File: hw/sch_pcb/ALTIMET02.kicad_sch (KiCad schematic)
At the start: 14 parts, among them IC1 MS561101BA03-50, J2 HEADER_2x03, J3 HEADER_2x05_PARALLEL

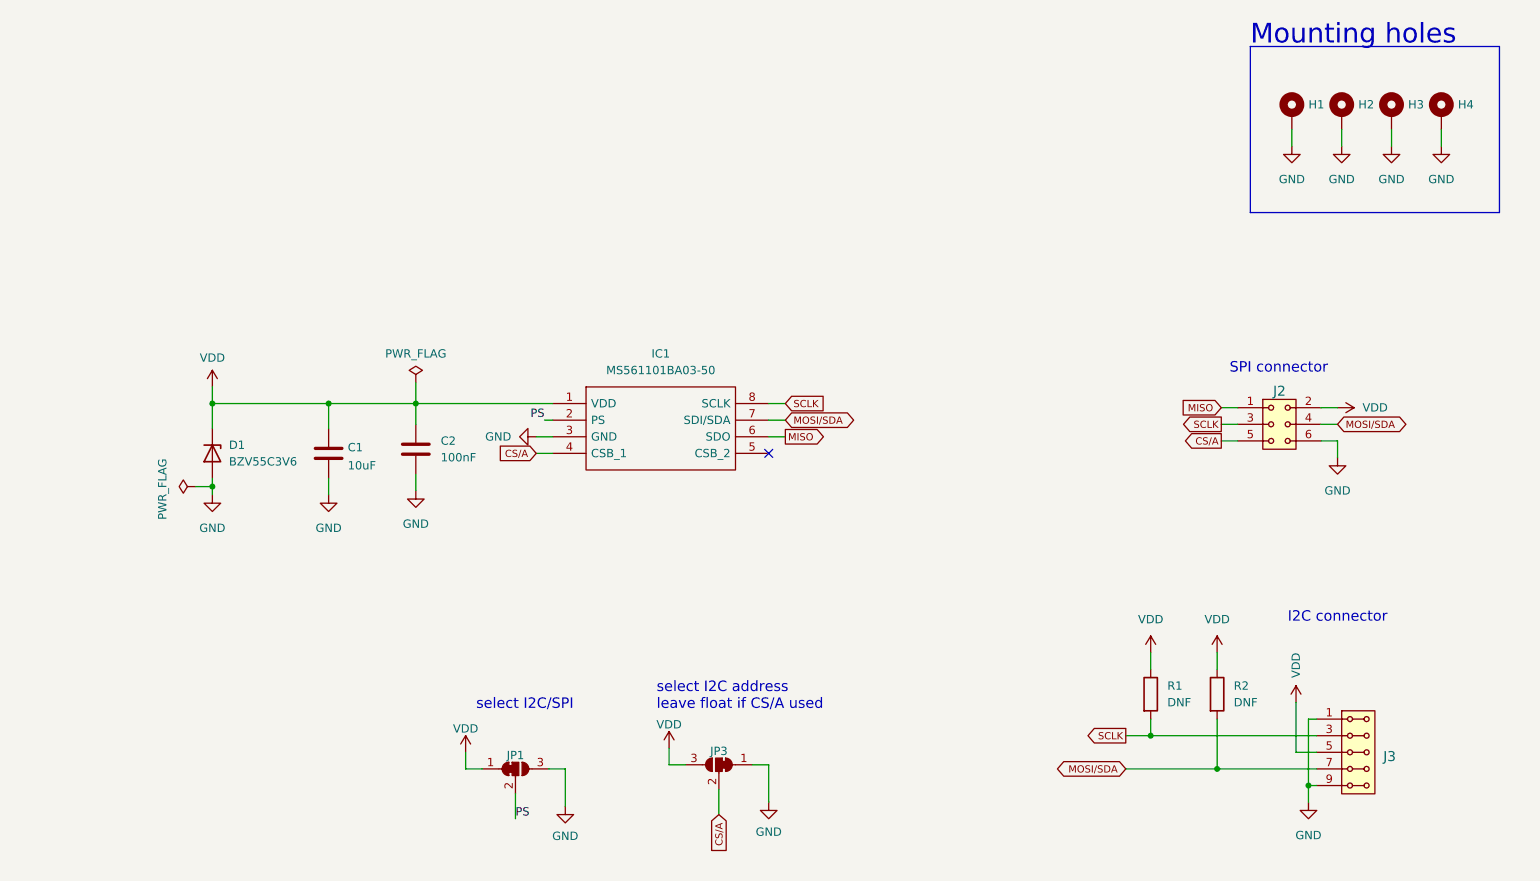
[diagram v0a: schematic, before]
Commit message: power connector added, SPI and I2C connectors modified, default I2C adrress changed
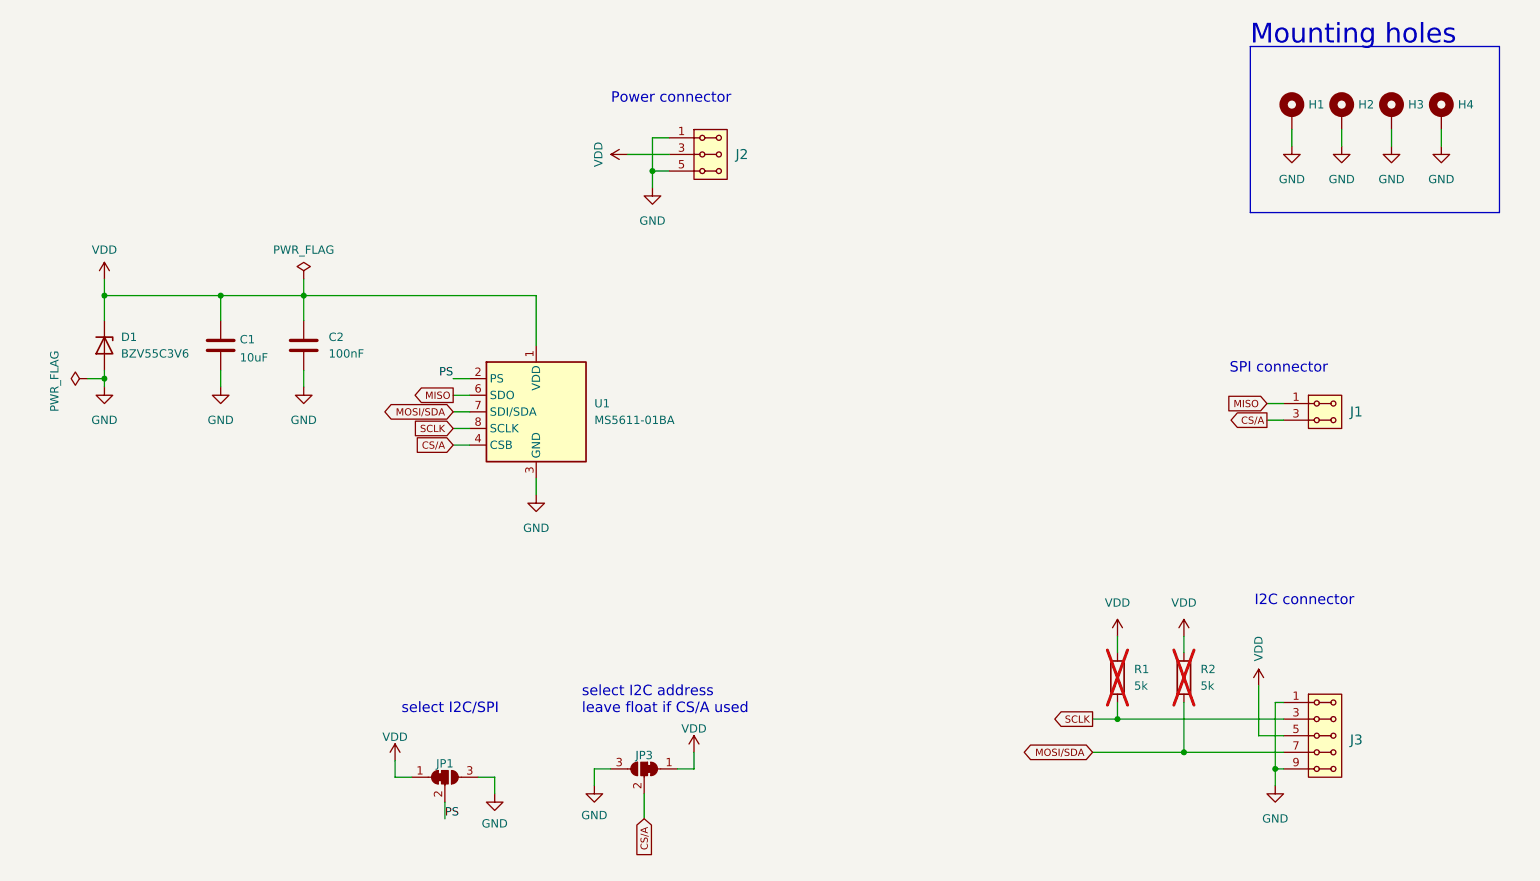
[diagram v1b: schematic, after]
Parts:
- removed IC1: MS561101BA03-50, KiCad:MS561101BA03-50, symbol MS561101BA03-50:MS561101BA03-50
- removed J2: HEADER_2x03, Mlab_Pin_Headers:Straight_2x03, symbol MLAB_HEADER:HEADER_2x03
- added J1: HEADER_2x02_PARALLEL, Mlab_Pin_Headers:Straight_2x02, symbol MLAB_HEADER:HEADER_2x02_PARALLEL
- added J2: HEADER_2x03_PARALLEL, Mlab_Pin_Headers:Straight_2x03, symbol MLAB_HEADER:HEADER_2x03_PARALLEL
- added U1: MS5611-01BA, Package_LGA:LGA-8_3x5mm_P1.25mm, symbol Sensor_Pressure:MS5611-01BA
- R1, R2: value DNF -> 5k; now not fitted
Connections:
- net CS/A: now also J1.3, J1.4, U1.4 (CSB), U1.5 (CSB)
- net GND: now also JP3.3 (B), J2.1, J2.2, J2.5, J2.6, U1.3 (GND); no longer JP3.1 (A)
- net MISO: now also J1.1, J1.2, U1.6 (SDO)
- net MOSI/SDA: now also U1.7 (SDI/SDA)
- net PS: now also U1.2 (PS)
- net SCLK: now also U1.8 (SCLK)
- net VDD: now also JP3.1 (A), J2.3, J2.4, U1.1 (VDD); no longer JP3.3 (B)
- no-connect marks 1 -> 0
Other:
- note added: "Power connector"
- moved on the sheet: C1, C2, D1, J3, JP1, JP3

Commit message: minor changes in layout, change diode
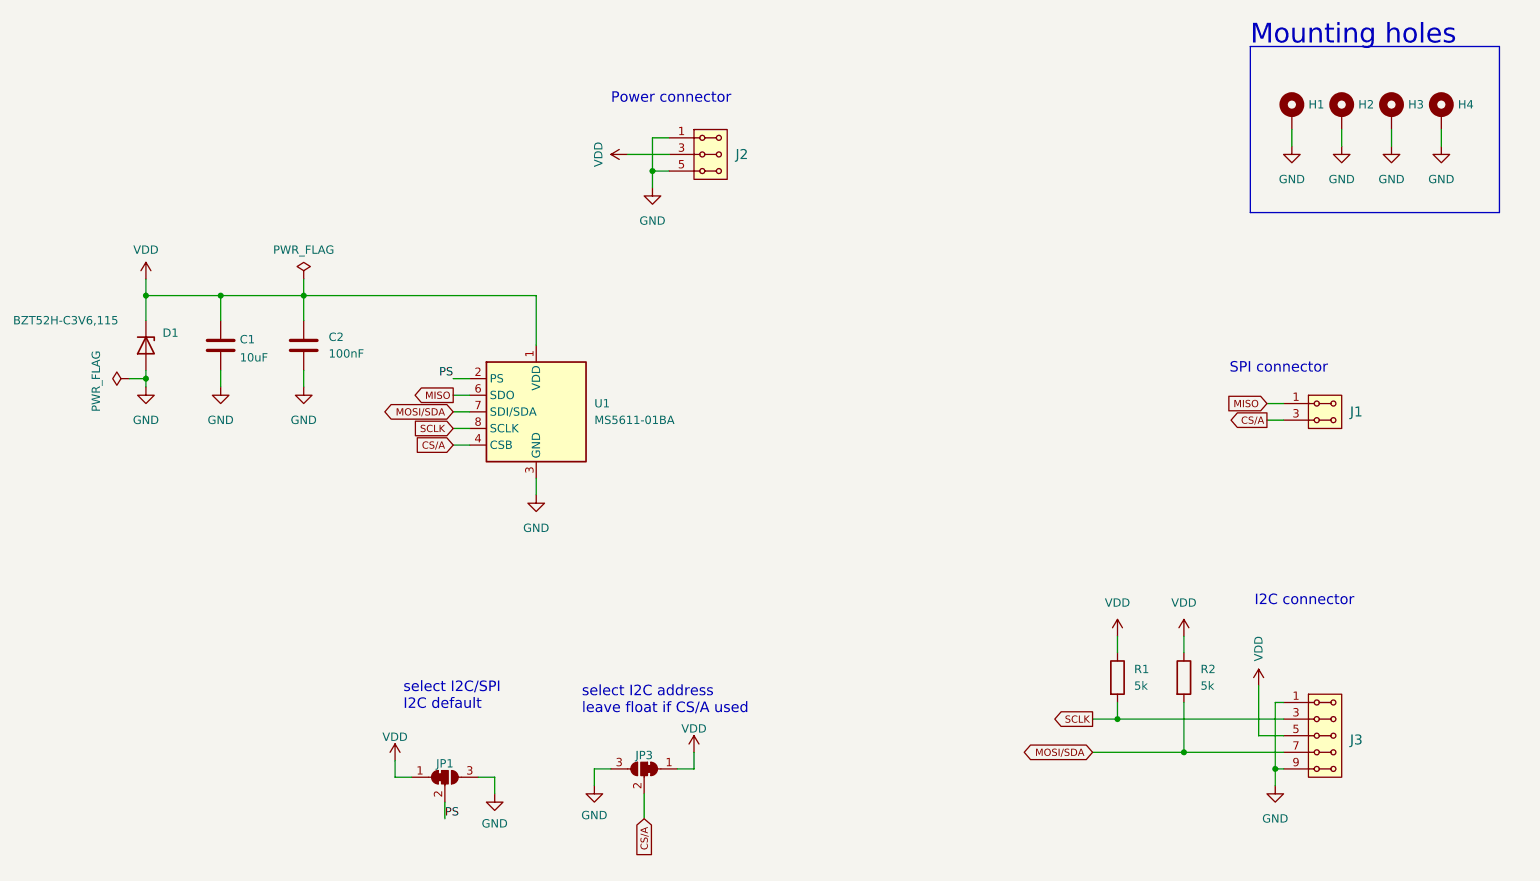
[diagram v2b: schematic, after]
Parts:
- D1: value BZV55C3V6 -> BZT52H-C3V6,115; footprint Mlab_D:Diode-MiniMELF_Standard -> Diode_SMD:D_SOD-123F
- R1, R2: now fitted
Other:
- note added: "select I2C/SPI I2C default"
- note removed: "select I2C/SPI"
- moved on the sheet: D1
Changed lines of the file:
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@@
   (junction (at 95.25 59.69) (diameter 0) (color 0 0 0 0)
   )
-  (junction (at 64.77 72.39) (diameter 0) (color 0 0 0 0)
+  (junction (at 71.12 72.39) (diameter 0) (color 0 0 0 0)
   )
   (junction (at 243.84 132.08) (diameter 0) (color 0 0 0 0)
@@
   (junction (at 219.71 124.46) (diameter 0) (color 0 0 0 0)
   )
-  (junction (at 64.77 59.69) (diameter 0) (color 0 0 0 0)
+  (junction (at 71.12 59.69) (diameter 0) (color 0 0 0 0)
   )
   (wire (pts (xy 82.55 59.69) (xy 82.55 63.5))
@@
     (stroke (width 0) (type default))
   )
-  (wire (pts (xy 62.23 72.39) (xy 64.77 72.39))
+  (wire (pts (xy 68.58 72.39) (xy 71.12 72.39))
     (stroke (width 0) (type default))
   )
@@
     (stroke (width 0) (type default))
   )
-  (wire (pts (xy 64.77 57.15) (xy 64.77 59.69))
+  (wire (pts (xy 71.12 57.15) (xy 71.12 59.69))
     (stroke (width 0) (type default))
   )
@@
     (stroke (width 0) (type default))
   )
-  (wire (pts (xy 64.77 72.39) (xy 64.77 73.66))
+  (wire (pts (xy 71.12 72.39) (xy 71.12 73.66))
     (stroke (width 0) (type default))
   )
@@
     (stroke (width 0) (type default))
   )
-  (wire (pts (xy 64.77 59.69) (xy 82.55 59.69))
+  (wire (pts (xy 71.12 59.69) (xy 82.55 59.69))
     (stroke (width 0) (type default))
   )
@@
     (stroke (width 0) (type default))
   )
-  (wire (pts (xy 64.77 63.5) (xy 64.77 59.69))
+  (wire (pts (xy 71.12 63.5) (xy 71.12 59.69))
     (stroke (width 0) (type default))
   )
@@
     (stroke (width 0) (type default))
   )
-  (wire (pts (xy 64.77 71.12) (xy 64.77 72.39))
+  (wire (pts (xy 71.12 71.12) (xy 71.12 72.39))
     (stroke (width 0) (type default))
   )
@@
     (stroke (width 0) (type default))
   )
-  (text "select I2C/SPI" (at 125.095 123.825 0)
-    (effects (font (size 1.6 1.6)) (justify right bottom))
+  (text "select I2C/SPI\nI2C default" (at 110.49 123.19 0)
+    (effects (font (size 1.6 1.6)) (justify left bottom))
   )
   (text "Mounting holes" (at 240.03 21.59 0)
@@
     )
   )
-  (symbol (lib_id "Device:D_Zener") (at 64.77 67.31 270) (unit 1)
-    (in_bom yes) (on_board yes) (dnp no) (fields_autoplaced)
-    (property "Reference" "D1" (at 67.31 66.0399 90)
-      (effects (font (size 1.27 1.27)) (justify left))
-    )
-    (property "Value" "BZV55C3V6" (at 67.31 68.5799 90)
-      (effects (font (size 1.27 1.27)) (justify left))
-    )
-    (property "Footprint" "Mlab_D:Diode-MiniMELF_Standard" (at 64.77 67.31 0)
-      (effects (font (size 1.27 1.27)) hide)
-    )
-    (property "Datasheet" "~" (at 64.77 67.31 0)
+  (symbol (lib_id "Device:D_Zener") (at 71.12 67.31 270) (unit 1)
+    (in_bom yes) (on_board yes) (dnp no)
+    (property "Reference" "D1" (at 73.66 65.405 90)
+      (effects (font (size 1.27 1.27)) (justify left))
+    )
+    (property "Value" "BZT52H-C3V6,115" (at 50.8 63.5 90)
+      (effects (font (size 1.27 1.27)) (justify left))
+    )
+    (property "Footprint" "Diode_SMD:D_SOD-123F" (at 71.12 67.31 0)
+      (effects (font (size 1.27 1.27)) hide)
+    )
+    (property "Datasheet" "~" (at 71.12 67.31 0)
       (effects (font (size 1.27 1.27)) hide)
     )
@@
     )
   )
-  (symbol (lib_id "power:GND") (at 64.77 73.66 0) (unit 1)
-    (in_bom yes) (on_board yes) (dnp no) (fields_autoplaced)
-    (property "Reference" "#PWR01" (at 64.77 80.01 0)
-      (effects (font (size 1.27 1.27)) hide)
-    )
-    (property "Value" "GND" (at 64.77 78.74 0)
-      (effects (font (size 1.27 1.27)))
-    )
-    (property "Footprint" "" (at 64.77 73.66 0)
-      (effects (font (size 1.27 1.27)) hide)
-    )
-    (property "Datasheet" "" (at 64.77 73.66 0)
+  (symbol (lib_id "power:GND") (at 71.12 73.66 0) (unit 1)
+    (in_bom yes) (on_board yes) (dnp no) (fields_autoplaced)
+    (property "Reference" "#PWR01" (at 71.12 80.01 0)
+      (effects (font (size 1.27 1.27)) hide)
+    )
+    (property "Value" "GND" (at 71.12 78.74 0)
+      (effects (font (size 1.27 1.27)))
+    )
+    (property "Footprint" "" (at 71.12 73.66 0)
+      (effects (font (size 1.27 1.27)) hide)
+    )
+    (property "Datasheet" "" (at 71.12 73.66 0)
       (effects (font (size 1.27 1.27)) hide)
     )
@@
   )
   (symbol (lib_id "Device:R") (at 229.87 118.11 0) (unit 1)
-    (in_bom yes) (on_board yes) (dnp yes) (fields_autoplaced)
+    (in_bom yes) (on_board yes) (dnp no) (fields_autoplaced)
     (property "Reference" "R2" (at 232.41 116.84 0)
       (effects (font (size 1.27 1.27)) (justify left))
@@
     )
   )
-  (symbol (lib_id "power:PWR_FLAG") (at 62.23 72.39 90) (unit 1)
+  (symbol (lib_id "power:PWR_FLAG") (at 68.58 72.39 90) (unit 1)
     (in_bom yes) (on_board yes) (dnp no)
-    (property "Reference" "#FLG02" (at 60.325 72.39 0)
-      (effects (font (size 1.27 1.27)) hide)
-    )
-    (property "Value" "PWR_FLAG" (at 57.15 77.47 0)
-      (effects (font (size 1.27 1.27)) (justify left))
-    )
-    (property "Footprint" "" (at 62.23 72.39 0)
-      (effects (font (size 1.27 1.27)) hide)
-    )
-    (property "Datasheet" "~" (at 62.23 72.39 0)
+    (property "Reference" "#FLG02" (at 66.675 72.39 0)
+      (effects (font (size 1.27 1.27)) hide)
+    )
+    (property "Value" "PWR_FLAG" (at 63.5 77.47 0)
+      (effects (font (size 1.27 1.27)) (justify left))
+    )
+    (property "Footprint" "" (at 68.58 72.39 0)
+      (effects (font (size 1.27 1.27)) hide)
+    )
+    (property "Datasheet" "~" (at 68.58 72.39 0)
       (effects (font (size 1.27 1.27)) hide)
     )
@@
     )
   )
-  (symbol (lib_id "power:VDD") (at 64.77 57.15 0) (unit 1)
+  (symbol (lib_id "power:VDD") (at 71.12 57.15 0) (unit 1)
     (in_bom yes) (on_board yes) (dnp no)
-    (property "Reference" "#PWR02" (at 64.77 60.96 0)
-      (effects (font (size 1.27 1.27)) hide)
-    )
-    (property "Value" "VDD" (at 64.77 52.705 0)
-      (effects (font (size 1.27 1.27)))
-    )
-    (property "Footprint" "" (at 64.77 57.15 0)
-      (effects (font (size 1.27 1.27)) hide)
-    )
-    (property "Datasheet" "" (at 64.77 57.15 0)
+    (property "Reference" "#PWR02" (at 71.12 60.96 0)
+      (effects (font (size 1.27 1.27)) hide)
+    )
+    (property "Value" "VDD" (at 71.12 52.705 0)
+      (effects (font (size 1.27 1.27)))
+    )
+    (property "Footprint" "" (at 71.12 57.15 0)
+      (effects (font (size 1.27 1.27)) hide)
+    )
+    (property "Datasheet" "" (at 71.12 57.15 0)
       (effects (font (size 1.27 1.27)) hide)
     )
@@
   )
   (symbol (lib_id "Device:R") (at 219.71 118.11 0) (unit 1)
-    (in_bom yes) (on_board yes) (dnp yes) (fields_autoplaced)
+    (in_bom yes) (on_board yes) (dnp no) (fields_autoplaced)
     (property "Reference" "R1" (at 222.25 116.84 0)
       (effects (font (size 1.27 1.27)) (justify left))

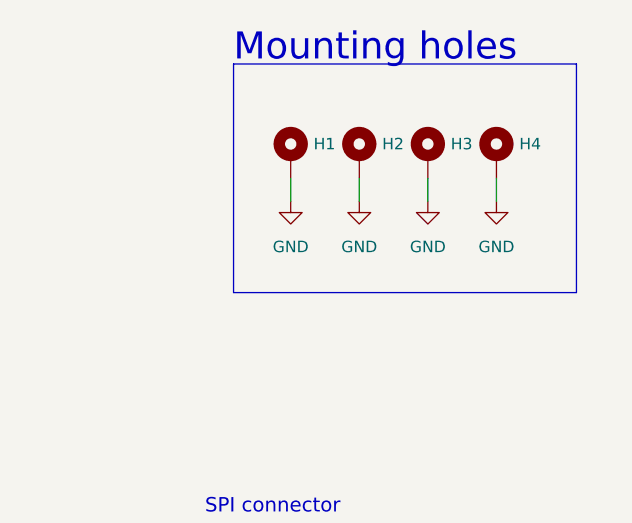
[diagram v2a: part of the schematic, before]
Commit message: add fiducial
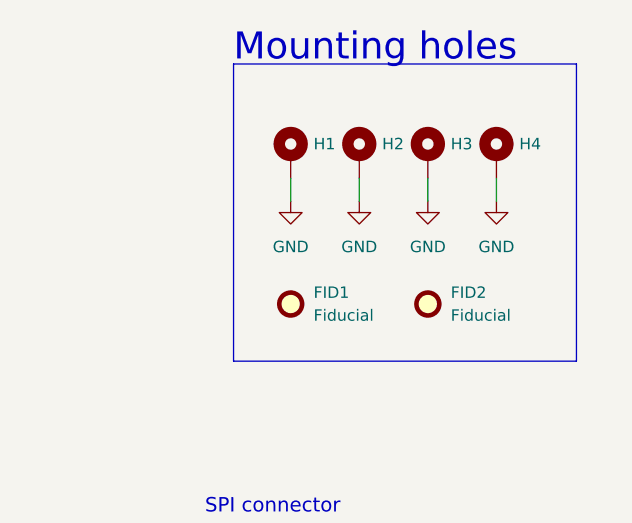
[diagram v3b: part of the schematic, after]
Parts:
- added FID1, FID2: Fiducial, Fiducial:Fiducial_1mm_Mask2mm, symbol Mechanical:Fiducial
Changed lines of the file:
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@@
     (stroke (width 0) (type default))
   )
-  (polyline (pts (xy 240.03 21.59) (xy 240.03 46.99))
+  (polyline (pts (xy 240.03 21.59) (xy 240.03 54.61))
     (stroke (width 0) (type default))
   )
@@
     (stroke (width 0) (type default))
   )
-  (polyline (pts (xy 278.13 21.59) (xy 278.13 46.99))
+  (polyline (pts (xy 278.13 21.59) (xy 278.13 54.61))
     (stroke (width 0) (type default))
   )
@@
     (stroke (width 0) (type default))
   )
-  (polyline (pts (xy 278.13 46.99) (xy 240.03 46.99))
+  (polyline (pts (xy 278.13 54.61) (xy 240.03 54.61))
     (stroke (width 0) (type default))
   )
@@
     (property "Intersheetrefs" "${INTERSHEET_REFS}" (at 147.3887 146.0329 90)
       (effects (font (size 1.1 1.1)) (justify right) hide)
+    )
+  )
+  (symbol (lib_id "Mechanical:Fiducial") (at 261.62 48.26 0) (unit 1)
+    (in_bom yes) (on_board yes) (dnp no) (fields_autoplaced)
+    (property "Reference" "FID2" (at 264.16 46.99 0)
+      (effects (font (size 1.27 1.27)) (justify left))
+    )
+    (property "Value" "Fiducial" (at 264.16 49.53 0)
+      (effects (font (size 1.27 1.27)) (justify left))
+    )
+    (property "Footprint" "Fiducial:Fiducial_1mm_Mask2mm" (at 261.62 48.26 0)
+      (effects (font (size 1.27 1.27)) hide)
+    )
+    (property "Datasheet" "~" (at 261.62 48.26 0)
+      (effects (font (size 1.27 1.27)) hide)
+    )
+    (instances
+      (project "ALTIMET02"
+        (path "/2b38a218-6231-4c8d-9ffe-42598e56f102"
+          (reference "FID2") (unit 1)
+        )
+      )
     )
   )
@@
         )
       )
+    )
+  )
+  (symbol (lib_id "Mechanical:Fiducial") (at 246.38 48.26 0) (unit 1)
+    (in_bom yes) (on_board yes) (dnp no) (fields_autoplaced)
+    (property "Reference" "FID1" (at 248.92 46.99 0)
+      (effects (font (size 1.27 1.27)) (justify left))
+    )
+    (property "Value" "Fiducial" (at 248.92 49.53 0)
+      (effects (font (size 1.27 1.27)) (justify left))
+    )
+    (property "Footprint" "Fiducial:Fiducial_1mm_Mask2mm" (at 246.38 48.26 0)
+      (effects (font (size 1.27 1.27)) hide)
+    )
+    (property "Datasheet" "~" (at 246.38 48.26 0)
+      (effects (font (size 1.27 1.27)) hide)
+    )
+    (instances
+      (project "ALTIMET02"
+        (path "/2b38a218-6231-4c8d-9ffe-42598e56f102"
+          (reference "FID1") (unit 1)
+        )
+      )

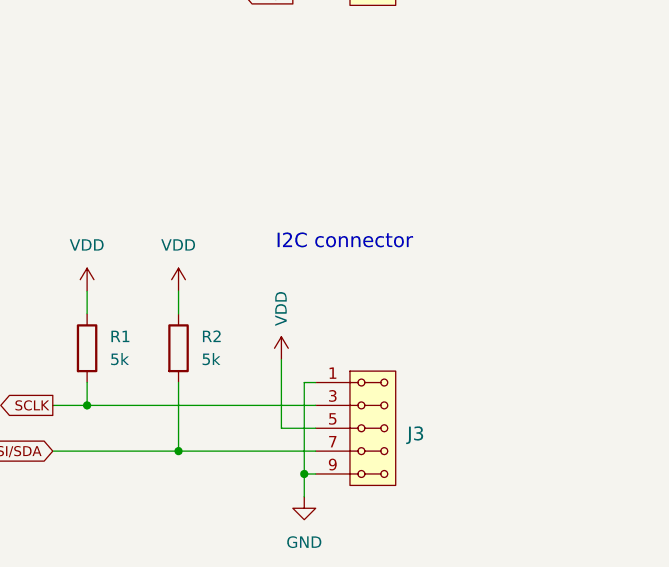
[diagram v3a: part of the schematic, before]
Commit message: Fix sharp trace. Improve silkscreen.
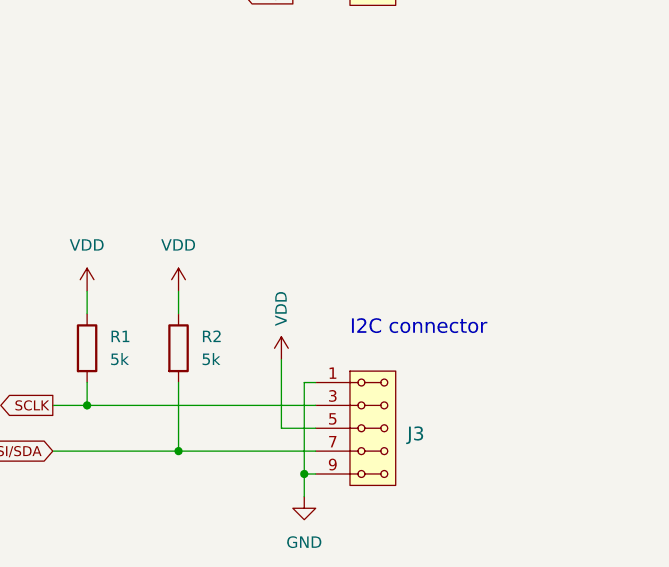
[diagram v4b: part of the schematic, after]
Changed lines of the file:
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@@
     (rev "A")
     (company "Marek Sommer")
-    (comment 1 "Digital altimeter  \\nand barometer sensor")
+    (comment 2 "Digital altimeter  \\nand barometer sensor\\nwith I²C or SPI interface")
   )
   (junction (at 82.55 59.69) (diameter 0) (color 0 0 0 0)
@@
     (effects (font (size 1.6 1.6)) (justify left bottom))
   )
-  (text "I2C connector" (at 240.665 107.315 0)
-    (effects (font (size 1.6 1.6)) (justify left bottom))
-  )
+  (text "I2C connector" (at 248.92 116.84 0)
+    (effects (font (size 1.6 1.6)) (justify left bottom))
+  )
